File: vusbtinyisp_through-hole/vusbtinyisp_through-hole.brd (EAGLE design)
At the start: 36.2 x 19 mm, 9 parts, among them J1 AVR_SPI_PRG_6NS, U1 TINY45-20-DIP

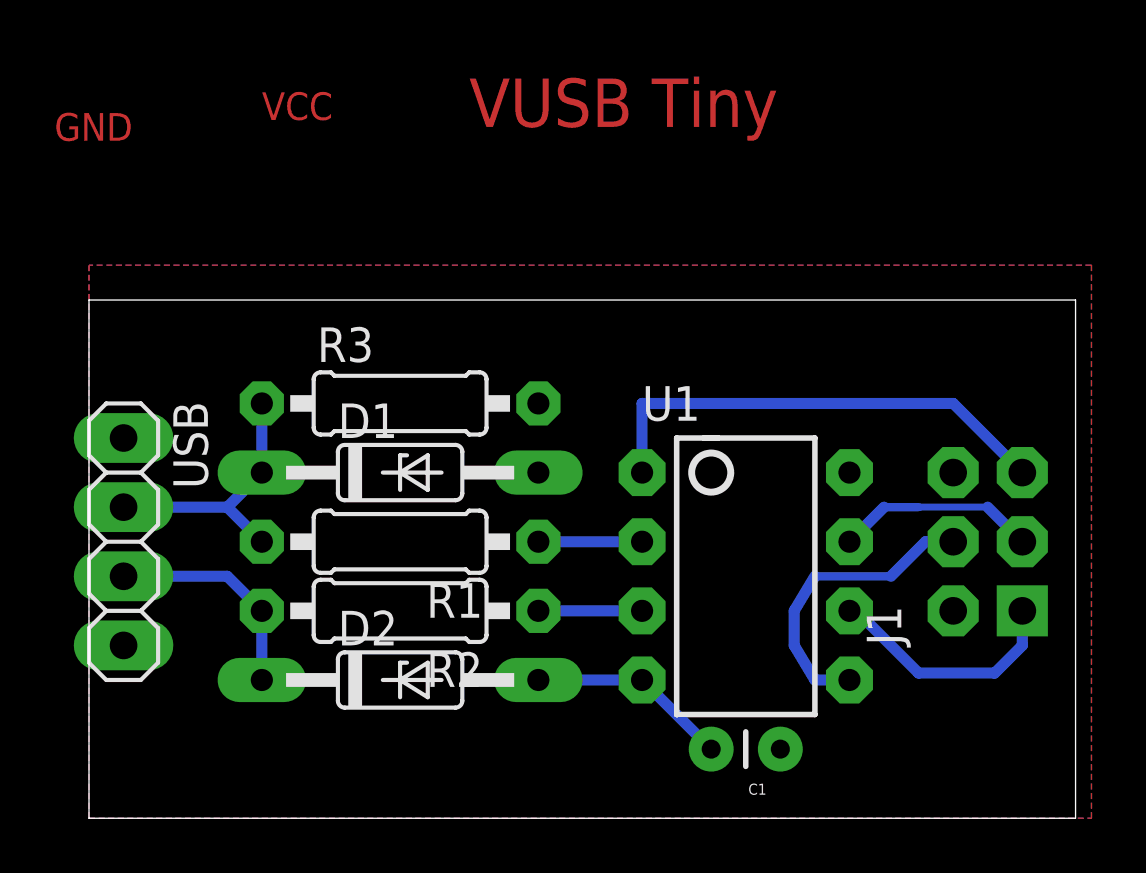
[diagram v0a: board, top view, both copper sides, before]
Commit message: moving all files to their own directories
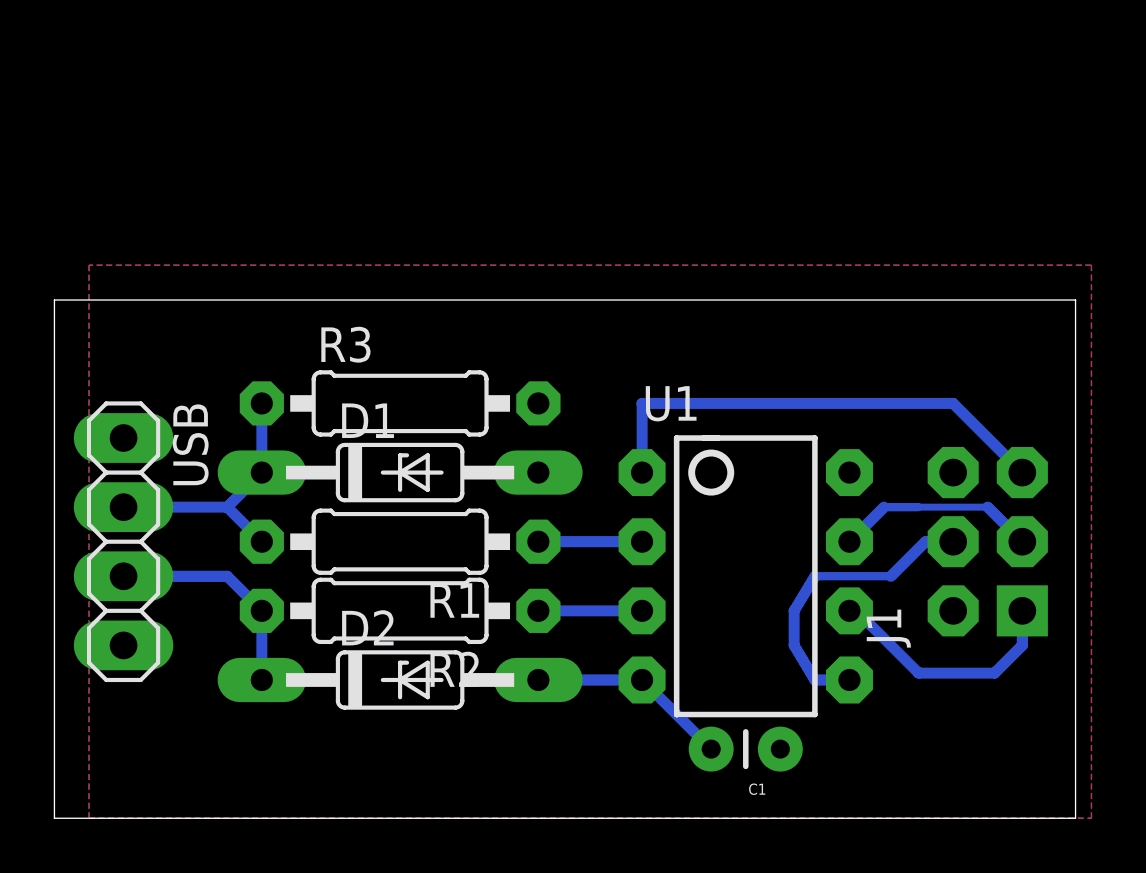
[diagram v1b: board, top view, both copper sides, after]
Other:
- board size 36.2 x 19 mm -> 37.5 x 19 mm
- board text removed: "GND"
- board text removed: "VCC"
- board text removed: "VUSB Tiny"
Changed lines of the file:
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@@
 <board>
 <plain>
-<wire x1="29.21" y1="29.21" x2="65.456" y2="29.21" width="0" layer="20"/>
+<wire x1="27.94" y1="29.21" x2="65.456" y2="29.21" width="0" layer="20"/>
 <wire x1="65.456" y1="29.21" x2="65.456" y2="48.25" width="0" layer="20"/>
-<wire x1="65.456" y1="48.25" x2="29.21" y2="48.25" width="0" layer="20"/>
-<wire x1="29.21" y1="48.25" x2="29.21" y2="29.21" width="0" layer="20"/>
-<text x="43.18" y="54.61" size="1.778" layer="1" font="vector">VUSB Tiny</text>
-<text x="35.56" y="55.372" size="1.016" layer="1" align="center-left">VCC</text>
-<text x="27.94" y="54.61" size="1.016" layer="1" align="center-left">GND</text>
+<wire x1="65.456" y1="48.25" x2="27.94" y2="48.25" width="0" layer="20"/>
+<wire x1="27.94" y1="48.25" x2="27.94" y2="29.21" width="0" layer="20"/>
 </plain>
 <attributes>
@@
 </signal>
 </signals>
+<errors>
+</errors>
 </board>
 </drawing>
